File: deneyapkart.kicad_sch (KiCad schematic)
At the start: 15 parts, among them J1 Conn_01x04_Pin, J2 Conn_01x02_Pin, J3 Conn_01x03_Pin, J4 Conn_01x03_Pin, J5 Conn_01x03_Pin, SW1 SW_MEC_5E, SW2 SW_MEC_5E

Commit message: footprintleri secildi
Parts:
- D1, D2: footprint (none) -> LED_THT:LED_D3.0mm
- J1: footprint (none) -> TerminalBlock_4Ucon:TerminalBlock_4Ucon_1x04_P3.50mm_Horizontal
- J2: footprint (none) -> TerminalBlock_4Ucon:TerminalBlock_4Ucon_1x02_P3.50mm_Horizontal
- J3, J4, J5: footprint (none) -> TerminalBlock_4Ucon:TerminalBlock_4Ucon_1x03_P3.50mm_Horizontal
- R1, R2, R3, R4, R5: footprint (none) -> Resistor_THT:R_Axial_DIN0204_L3.6mm_D1.6mm_P5.08mm_Horizontal
- SW1, SW2: footprint (none) -> Button_Switch_THT:SW_Tactile_Straight_KSA0Axx1LFTR
- U1: footprint (none) -> deneyapkart:deneyapkart
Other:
- note added: "UART"
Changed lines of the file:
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@@
+		)
+	)
+	(text "UART"
+		(exclude_from_sim no)
+		(at 101.854 76.2 0)
+		(effects
+			(font
+				(size 1.27 1.27)
+			)
 		)
 	)
@@
 			)
 		)
-		(property "Footprint" ""
+		(property "Footprint" "Button_Switch_THT:SW_Tactile_Straight_KSA0Axx1LFTR"
 			(at 25.4 17.78 0)
 			(effects
@@
 			)
 		)
-		(property "Footprint" ""
+		(property "Footprint" "LED_THT:LED_D3.0mm"
 			(at 62.23 24.13 0)
 			(effects
@@
 			)
 		)
-		(property "Footprint" ""
+		(property "Footprint" "deneyapkart:deneyapkart"
 			(at 39.37 101.6 0)
 			(effects
@@
 			)
 		)
-		(property "Footprint" ""
+		(property "Footprint" "TerminalBlock_4Ucon:TerminalBlock_4Ucon_1x03_P3.50mm_Horizontal"
 			(at 116.84 49.53 0)
 			(effects
@@
 			)
 		)
-		(property "Footprint" ""
+		(property "Footprint" "TerminalBlock_4Ucon:TerminalBlock_4Ucon_1x03_P3.50mm_Horizontal"
 			(at 87.63 82.55 0)
 			(effects
@@
 			)
 		)
-		(property "Footprint" ""
+		(property "Footprint" "Resistor_THT:R_Axial_DIN0204_L3.6mm_D1.6mm_P5.08mm_Horizontal"
 			(at 36.83 27.178 90)
 			(effects
@@
 			)
 		)
-		(property "Footprint" ""
+		(property "Footprint" "TerminalBlock_4Ucon:TerminalBlock_4Ucon_1x02_P3.50mm_Horizontal"
 			(at 130.81 17.78 0)
 			(effects
@@
 			)
 		)
-		(property "Footprint" ""
+		(property "Footprint" "LED_THT:LED_D3.0mm"
 			(at 59.69 49.53 0)
 			(effects
@@
 			)
 		)
-		(property "Footprint" ""
+		(property "Footprint" "Resistor_THT:R_Axial_DIN0204_L3.6mm_D1.6mm_P5.08mm_Horizontal"
 			(at 71.12 25.908 90)
 			(effects
@@
 			)
 		)
-		(property "Footprint" ""
+		(property "Footprint" "Resistor_THT:R_Axial_DIN0204_L3.6mm_D1.6mm_P5.08mm_Horizontal"
 			(at 68.58 51.308 90)
 			(effects
@@
 			)
 		)
-		(property "Footprint" ""
+		(property "Footprint" "TerminalBlock_4Ucon:TerminalBlock_4Ucon_1x03_P3.50mm_Horizontal"
 			(at 90.17 50.8 0)
 			(effects
@@
 			)
 		)
-		(property "Footprint" ""
+		(property "Footprint" "Resistor_THT:R_Axial_DIN0204_L3.6mm_D1.6mm_P5.08mm_Horizontal"
 			(at 121.412 26.67 90)
 			(effects
@@
 			)
 		)
-		(property "Footprint" ""
+		(property "Footprint" "Resistor_THT:R_Axial_DIN0204_L3.6mm_D1.6mm_P5.08mm_Horizontal"
 			(at 36.83 52.578 90)
 			(effects
@@
 			)
 		)
-		(property "Footprint" ""
+		(property "Footprint" "TerminalBlock_4Ucon:TerminalBlock_4Ucon_1x04_P3.50mm_Horizontal"
 			(at 104.14 22.86 0)
 			(effects
@@
 			)
 		)
-		(property "Footprint" ""
+		(property "Footprint" "Button_Switch_THT:SW_Tactile_Straight_KSA0Axx1LFTR"
 			(at 25.4 43.18 0)
 			(effects

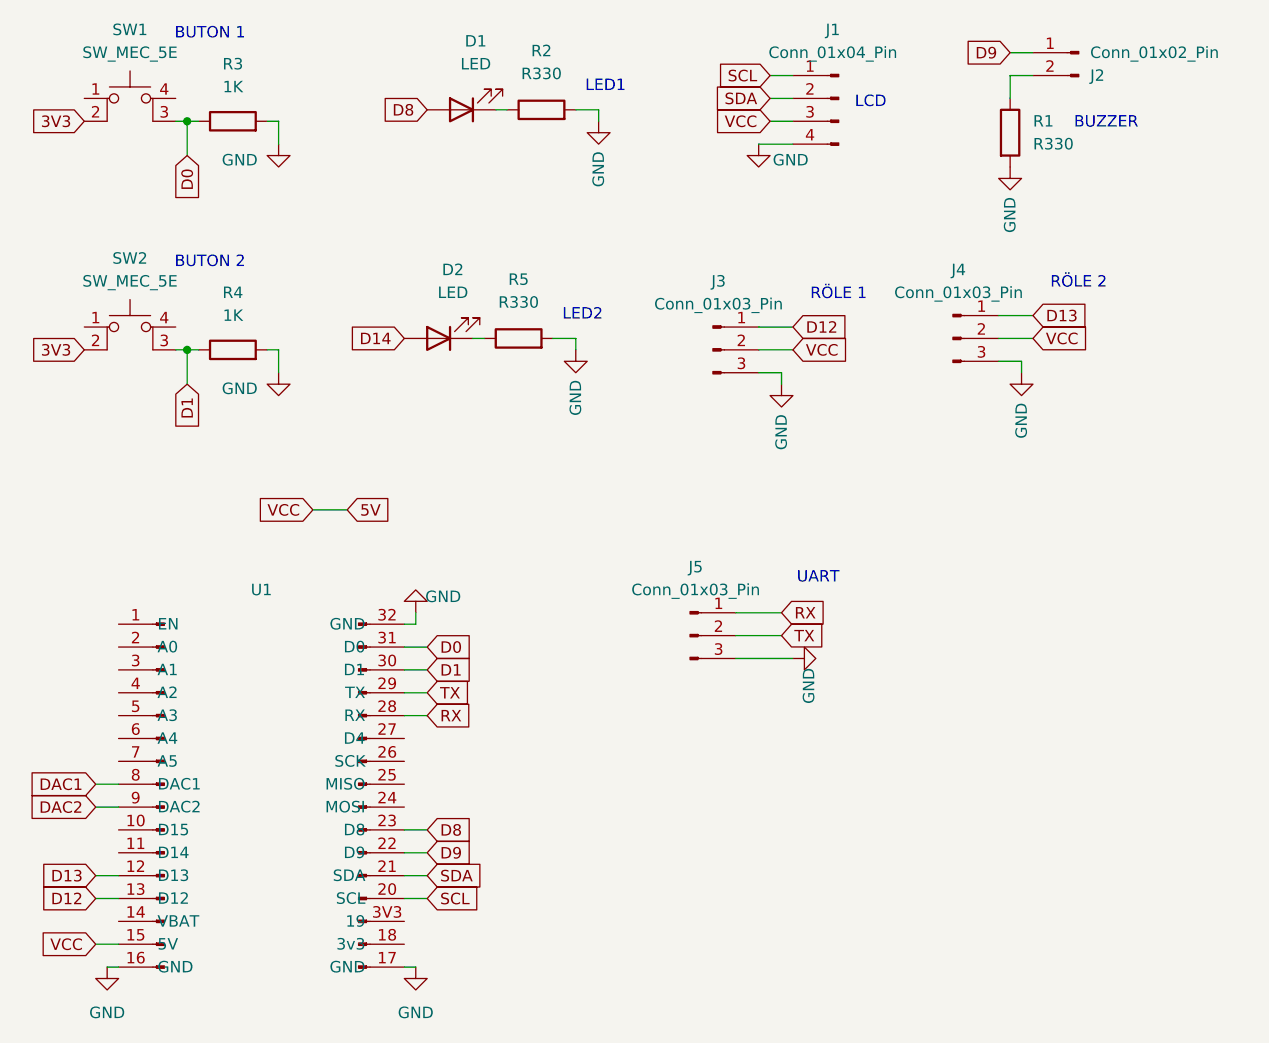
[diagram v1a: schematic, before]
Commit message: footprintler düzenlendi . bomlist olusturuldu, ground plane yollar cizildi
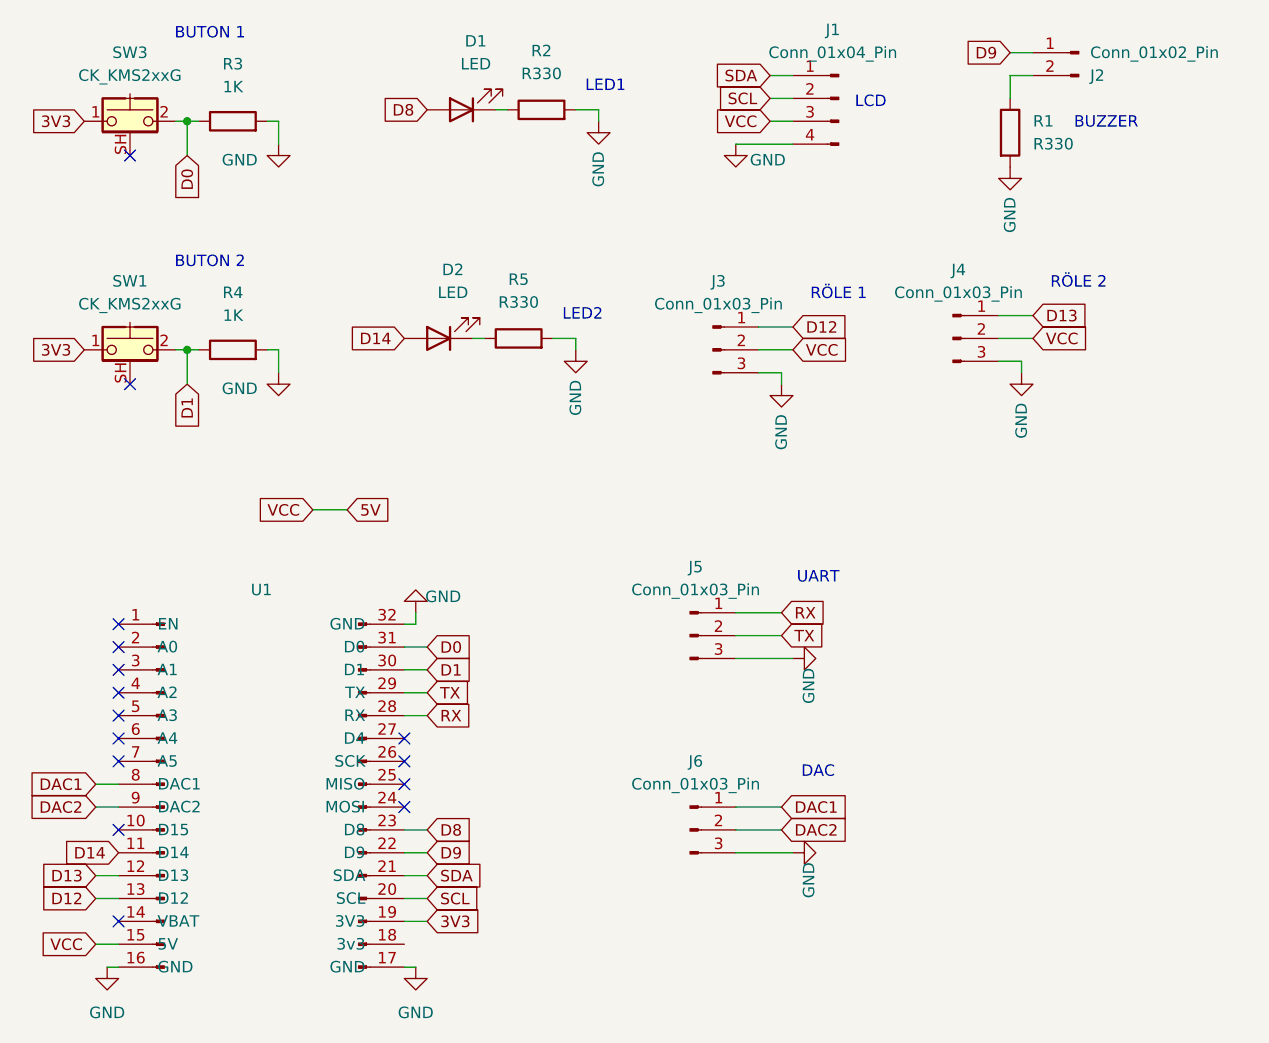
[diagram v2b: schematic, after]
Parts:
- removed SW1, SW2: SW_MEC_5E, Button_Switch_THT:SW_Tactile_Straight_KSA0Axx1LFTR, symbol Switch:SW_MEC_5E
- added J6: Conn_01x03_Pin, TerminalBlock_4Ucon:TerminalBlock_4Ucon_1x03_P3.50mm_Horizontal, symbol Connector:Conn_01x03_Pin
- added SW1, SW3: CK_KMS2xxG, Button_Switch_THT:SW_PUSH_6mm_H4.3mm, symbol Switch:CK_KMS2xxG
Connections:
- net 3V3: now also U1.19 (3V3), SW1.1, SW3.1
- net D0: now also SW3.2
- net D1: now also SW1.2
- net D14: now also U1.11 (D14)
- net DAC1: now also J6.1 (Pin_1)
- net DAC2: now also J6.2 (Pin_2)
- net GND: now also J6.3 (Pin_3)
- net SCL: now also J1.2 (Pin_2); no longer J1.1 (Pin_1)
- net SDA: now also J1.1 (Pin_1); no longer J1.2 (Pin_2)
- no-connect marks 0 -> 15
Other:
- note added: "DAC"
